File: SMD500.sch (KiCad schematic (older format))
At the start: 603 parts, among them CN1 DB9-M, CN10 PJRAN1X1U03AUX(YELLOW), CN11 2x17, CN12 2-171825-4, CN13 1x8HEADER, CN14 2-171825-4, CN15 Conn_01x04, CN2 DB9-M, CN3 PJRAN1X1U03AUX(RED), CN4 PJRAN1X1U02AUX(WHITE), CN45 Conn_01x04, CN5 DB23_Female_MountingHoles, CN6 DB25P, CN7 DB25S, CN8 SQ&RNDDIN, CN9 DB23, P1 EDGE86, P9 Conn_02x28_Odd_Even, Q301 MMBT3906-TP, Q321 PMBF4391, Q331 PMBF4391, Q501 MMBT3904-TP, Q502 MMBT3906-TP, Q503 MMBT3906-TP, Q711 MMBT3904-TP, U1 68000D, U10 SN74LS244DW, U11 SN74LS373DW, U12 SN74LS244DW, U13 SN74LS373DW, U14 TL084, U15 SN74LS157DR, U16 HYB514256B, U17 HYB514256B, U18 HYB514256B, U19 HYB514256B, U2.1 8375_FatAgnus2MB, U2.2 8372_FatAgnus1MB, U20 HYB514256B, U201 HYB5118160BSJ, U21 HYB514256B, U22 HYB514256B, U23 HYB514256B, U3 8364_Paula, U32 MC74AC139DR2G, U33 SN74F258D, U33.1 SN74F04DR, U34 SN74LS373DW, U35 N74F244D, U36 SN74LS05DR, U37 74LS32, U38 MAX1488ECSD+, U39 MAX1489ECSD+, U4 8373_DeniseECS, U40 SN74HCT245DWR, U41 SN74HCT245DWR, U42 NE555DR, U45 AD723ARUZ, U5 5719_Gary, U6 ROM_SOCKET, U7 8520_CIA, U8 8520_CIA, U9 RTC72421, X1 ACO-28.37516MHz, Y460 17.734 475 MHz 18 pF, Y9 LFXTAL002995Bulk

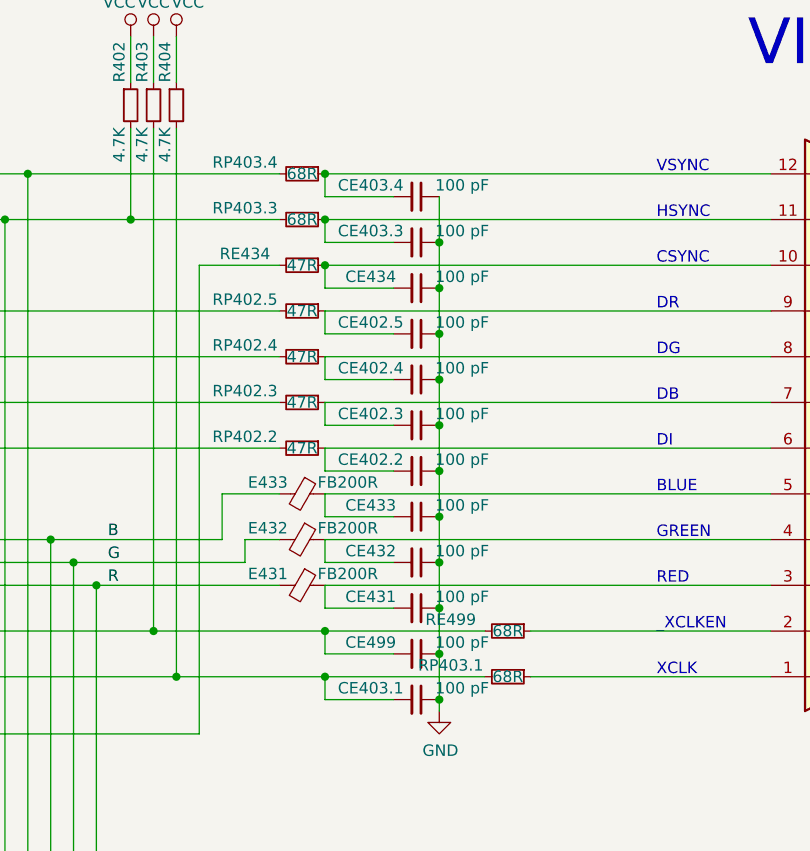
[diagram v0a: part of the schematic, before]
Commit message: Add files via upload
Minor revision to fix problem with solder mask
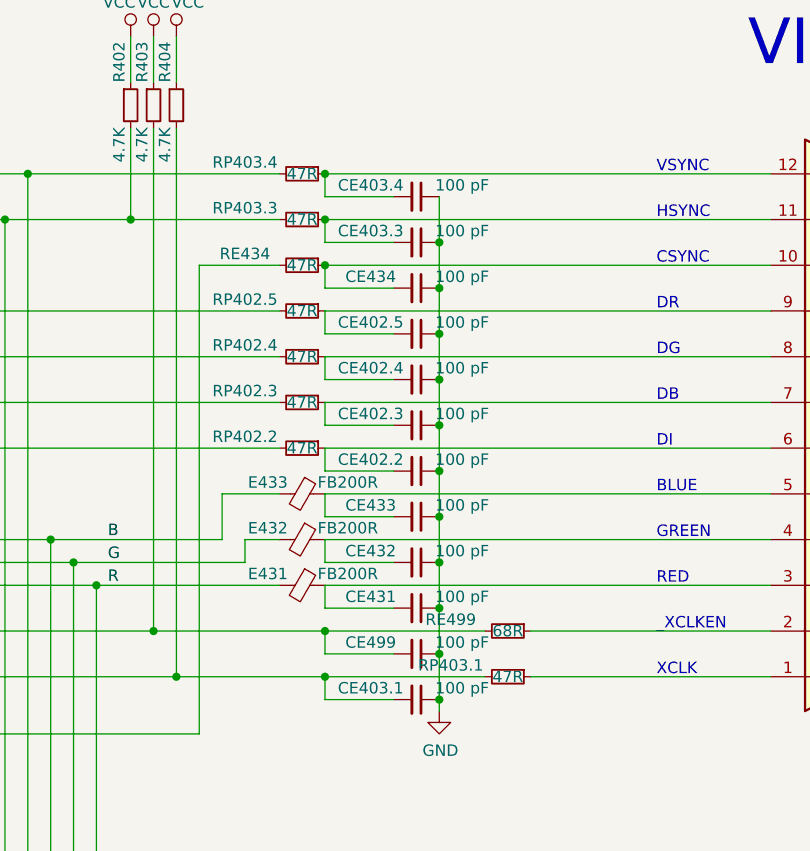
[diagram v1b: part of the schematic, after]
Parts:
- RP403.1, RP403.3, RP403.4: value 68R -> 47R
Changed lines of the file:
@@
 P 41250 4200
 F 0 "RP403.3" V 41200 3950 50  0000 C CNN
-F 1 "68R" V 41250 4200 50  0000 C CNN
+F 1 "47R" V 41250 4200 50  0000 C CNN
 F 2 "Resistor_SMD:R_0805_2012Metric_Pad1.15x1.40mm_HandSolder" H 41250 4200 50  0001 C CNN
 F 3 "~" H 41250 4200 50  0001 C CNN
@@
 P 41250 4000
 F 0 "RP403.4" V 41200 3750 50  0000 C CNN
-F 1 "68R" V 41250 4000 50  0000 C CNN
+F 1 "47R" V 41250 4000 50  0000 C CNN
 F 2 "Resistor_SMD:R_0805_2012Metric_Pad1.15x1.40mm_HandSolder" H 41250 4000 50  0001 C CNN
 F 3 "~" H 41250 4000 50  0001 C CNN
@@
 P 42150 6200
 F 0 "RP403.1" V 42100 5950 50  0000 C CNN
-F 1 "68R" V 42150 6200 50  0000 C CNN
+F 1 "47R" V 42150 6200 50  0000 C CNN
 F 2 "Resistor_SMD:R_0805_2012Metric_Pad1.15x1.40mm_HandSolder" H 42150 6200 50  0001 C CNN
 F 3 "~" H 42150 6200 50  0001 C CNN
